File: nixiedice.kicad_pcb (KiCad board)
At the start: 2 copper layers, 127 x 63.5 mm, 51 parts, among them CON1 BARREL_JACK, M1 1pin, M2 1pin, M3 1pin, M4 1pin, P1 USB_OTG, P2 USB_A, P3 ARDUINO PRO MICRO, P8 CONN_01X04, Q1 MPSA42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

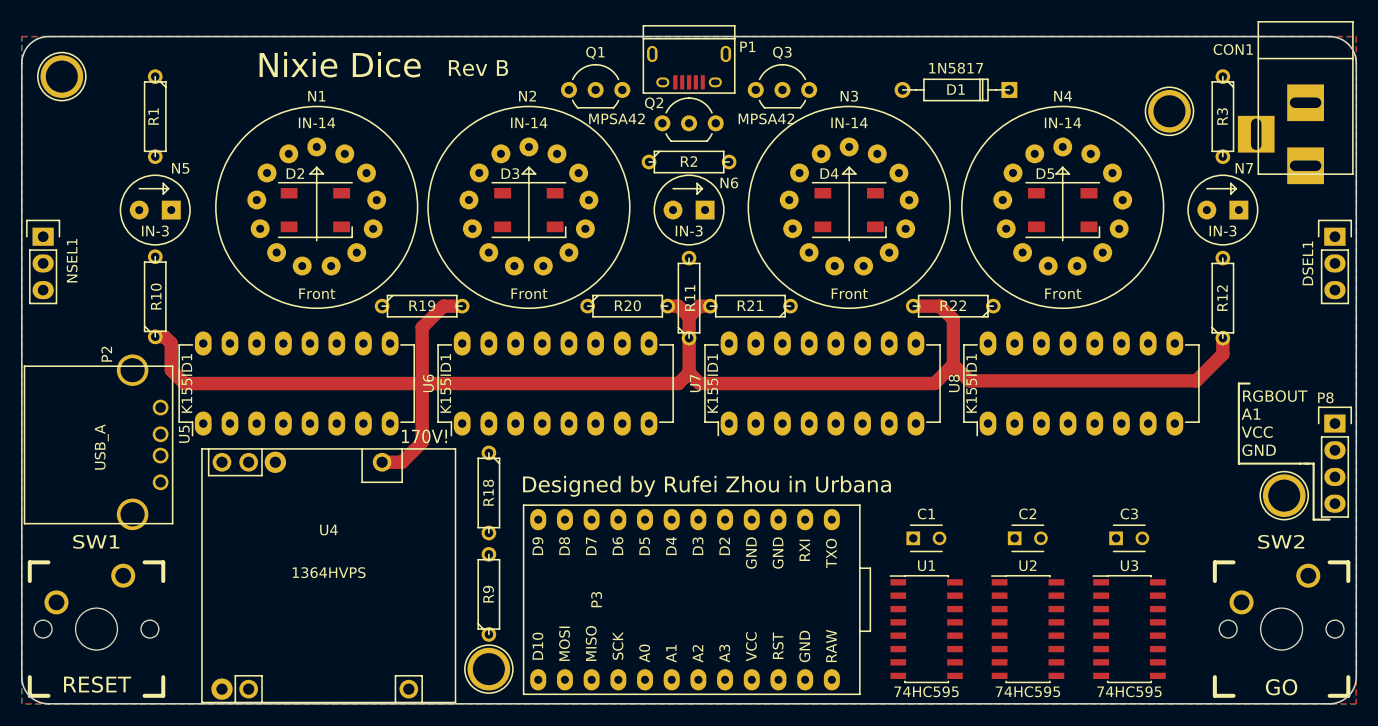
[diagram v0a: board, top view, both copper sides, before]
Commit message: change microusb connector to use smd pads
also add line on front silkscreen to plug this schweet repo
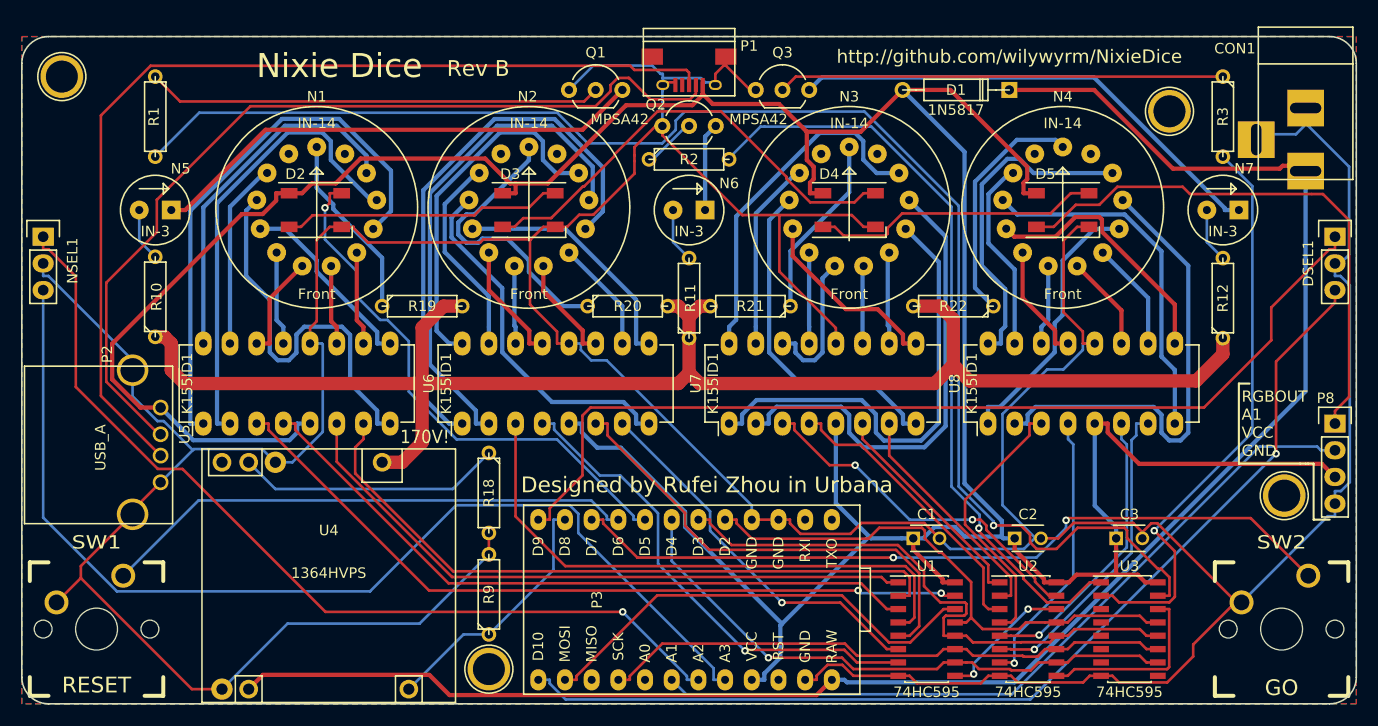
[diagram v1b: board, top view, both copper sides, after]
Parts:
- P1: footprint Connect:USB_Micro-B -> Custom:USB_Micro-B
- moved CON1 0.51 mm to (122.2, 6.60)
- moved R2 0.25 mm to (63.5, 11.7)
- moved P1 0.25 mm to (63.5, 3.05)
- moved Q2 0.25 mm to (61.0, 8.51)
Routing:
- net GND: track 0.00 -> 476.7 mm
- net VCC: track 0.00 -> 331.8 mm
- net /RAW: track 0.00 -> 167.0 mm
- net Net-(R1-Pad2): track 0.00 -> 140.8 mm, vias 0 -> 1
- net /A3: track 0.00 -> 101.4 mm
- net /D10: track 0.00 -> 98.8 mm, vias 0 -> 1
- net /D+: track 0.00 -> 93.9 mm
- net /D9: track 0.00 -> 93.5 mm
- net /A2: track 0.00 -> 86.9 mm, vias 0 -> 1
- net /D-: track 0.00 -> 84.9 mm
- net /BTN_GO: track 0.00 -> 74.2 mm, vias 0 -> 2
- net /T1INA: track 0.00 -> 73.6 mm, vias 0 -> 2
- net /A1: track 0.00 -> 73.6 mm
- net Net-(R2-Pad2): track 0.00 -> 73.1 mm, vias 0 -> 1
- net /T1IND: track 0.00 -> 66.2 mm
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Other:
- board text added: "http://github.com/wilywyrm/NixieDice"
